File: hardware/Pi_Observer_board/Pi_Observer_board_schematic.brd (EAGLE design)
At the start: 160 x 100 mm, 17 parts, among them Q1 BC548B, U1 DS18B20, U2 DS18B20, X1 RASPI_GPIO_B+#_PIN

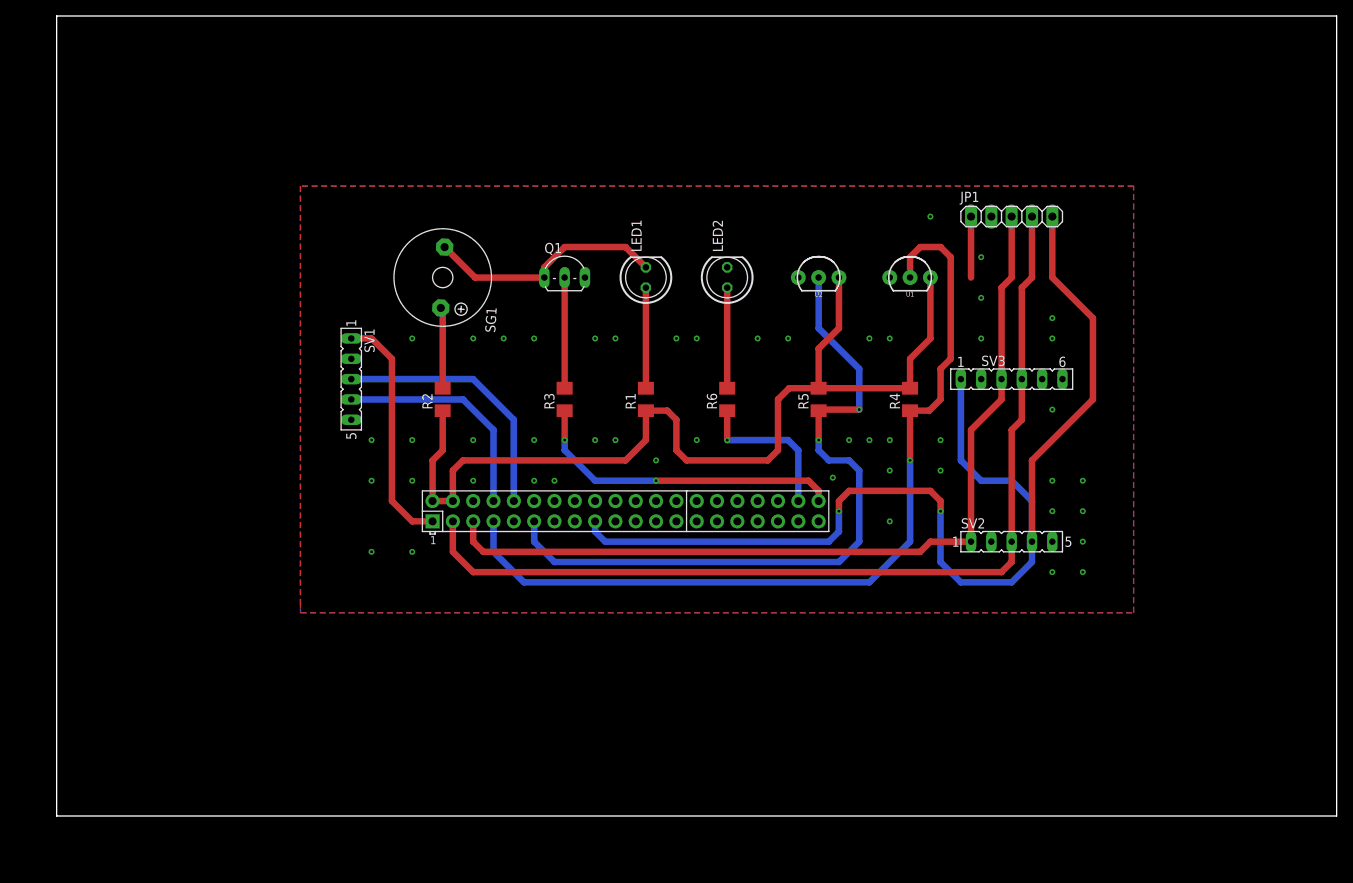
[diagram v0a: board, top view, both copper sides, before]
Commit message: Advance board and chnage gpio pins
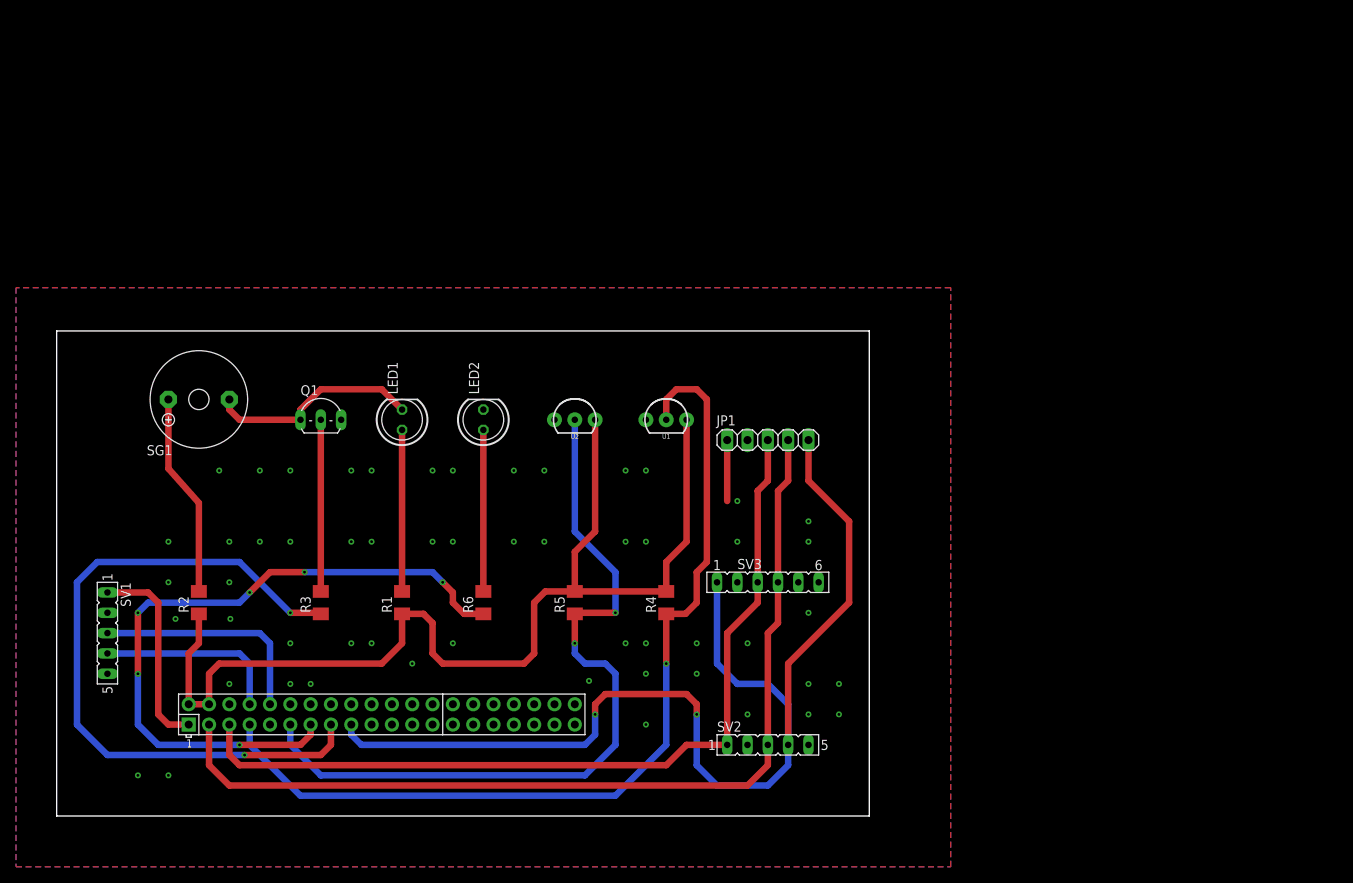
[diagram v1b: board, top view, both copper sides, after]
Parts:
- JP1: value (none) -> RTC
- LED1: value (none) -> RED
- LED2: value (none) -> GREEN
- R1: value (none) -> 180
- R2, R6: value (none) -> 150
- R3: value (none) -> 1k
- R4, R5: value (none) -> 4k7
- SV2: value (none) -> HUMIDITY
- SV3: value (none) -> PRESSURE
- moved SV1 44.0 mm to (6.35, 22.9)
- moved JP1 41.3 mm to (88.9, 47.0)
- moved R1 39.7 mm to (43.2, 26.7)
- moved R2 39.7 mm to (17.8, 26.7)
- moved R3 39.7 mm to (33.0, 26.7)
- moved R4 39.7 mm to (76.2, 26.7)
- moved R5 39.7 mm to (64.8, 26.7)
- moved X1 39.7 mm to (40.6, 12.7)
- moved R6 39.7 mm to (53.3, 26.7)
- moved SV2 39.7 mm to (88.9, 8.89)
- moved SV3 39.7 mm to (88.9, 29.2)
- moved U1 35.3 mm to (76.2, 49.5)
- moved U2 35.3 mm to (64.8, 49.5)
- moved LED1 35.3 mm to (43.2, 49.5)
- moved LED2 35.3 mm to (53.3, 49.5)
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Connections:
- removed net GPIO20: R6.1, X1.38
- removed net GPIO21: R3.1, X1.40
- new net GPIO22: R3.1, X1.15
- new net GPIO27: R6.1, X1.13
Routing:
- net GPIO22: track 0.00 -> 88.4 mm, vias 0 -> 2
- net GPIO27: track 0.00 -> 86.6 mm, vias 0 -> 6
- net GPIO21: track 40.1 -> 0.00 mm, vias 2 -> 0
- net GPIO20: track 19.4 -> 0.00 mm, vias 1 -> 0
- net N$2: track 10.1 -> 25.4 mm
- net +5V: track 122.8 -> 138.1 mm
- net GPIO17: track 89.0 -> 97.7 mm
- net GPIO04: track 107.3 -> 115.2 mm
- net N$5: track 13.8 -> 21.5 mm
- net N$9: track 12.6 -> 20.2 mm
- net N$3: track 12.6 -> 20.2 mm
- net +3V3: track 176.2 -> 168.8 mm
- net TX: track 28.2 -> 23.4 mm
- net RX: track 32.6 -> 28.5 mm
- net N$1: track 30.1 -> 26.8 mm
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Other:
- board size 160 x 100 mm -> 101.6 x 60.6 mm
